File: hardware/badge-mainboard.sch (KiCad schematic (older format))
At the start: 13 parts

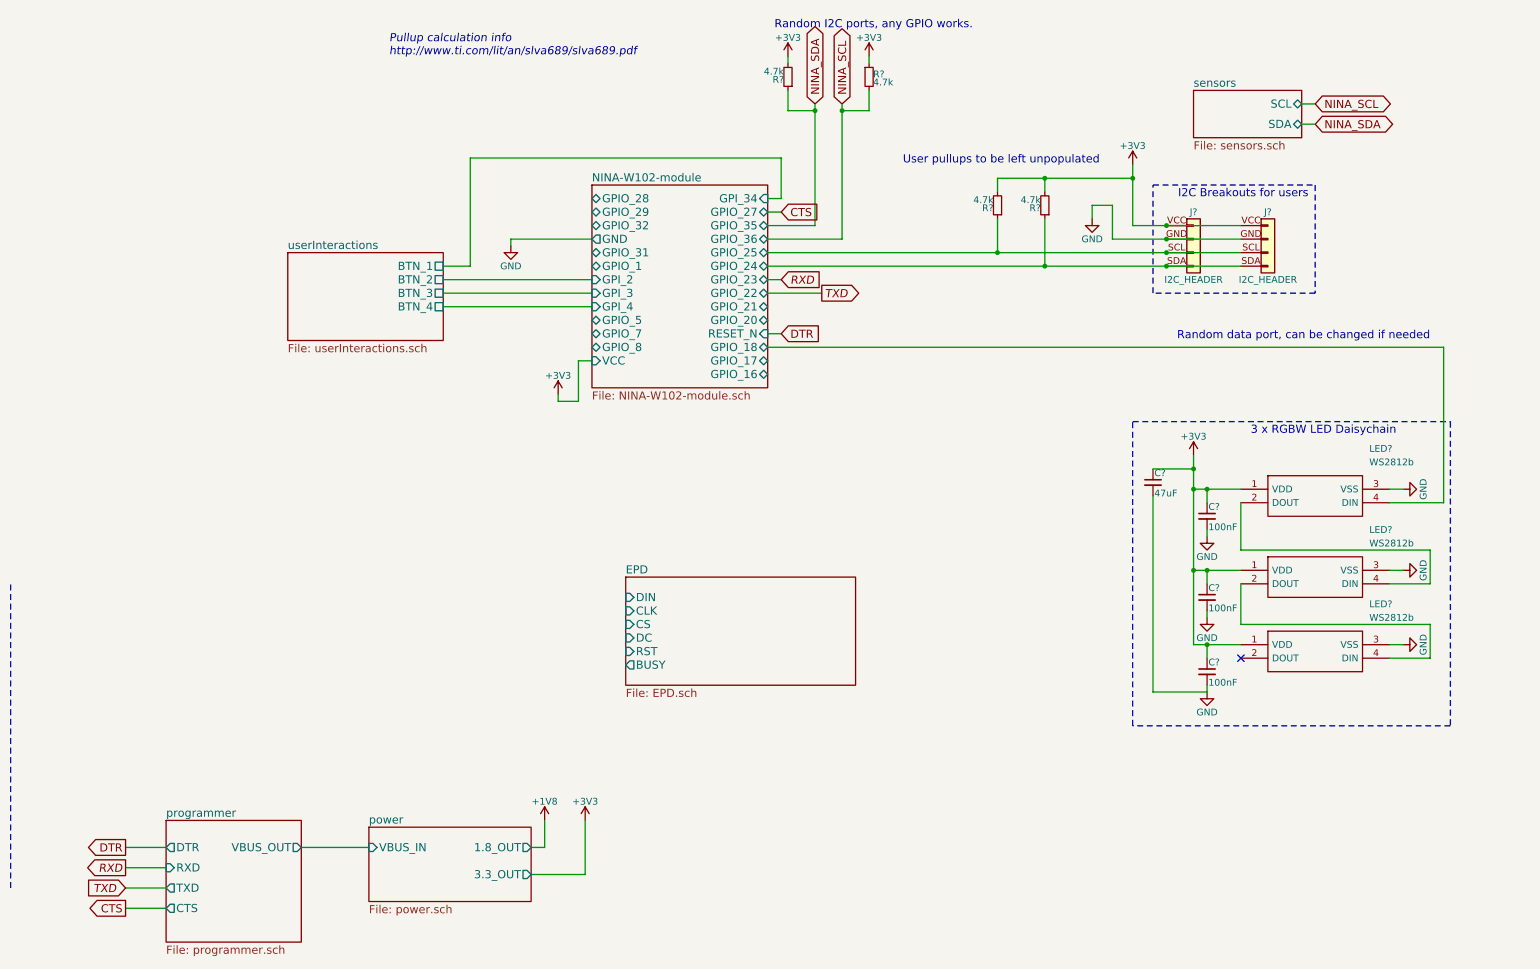
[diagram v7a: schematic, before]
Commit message: moved sensor to module board, removed programmer as external will be used
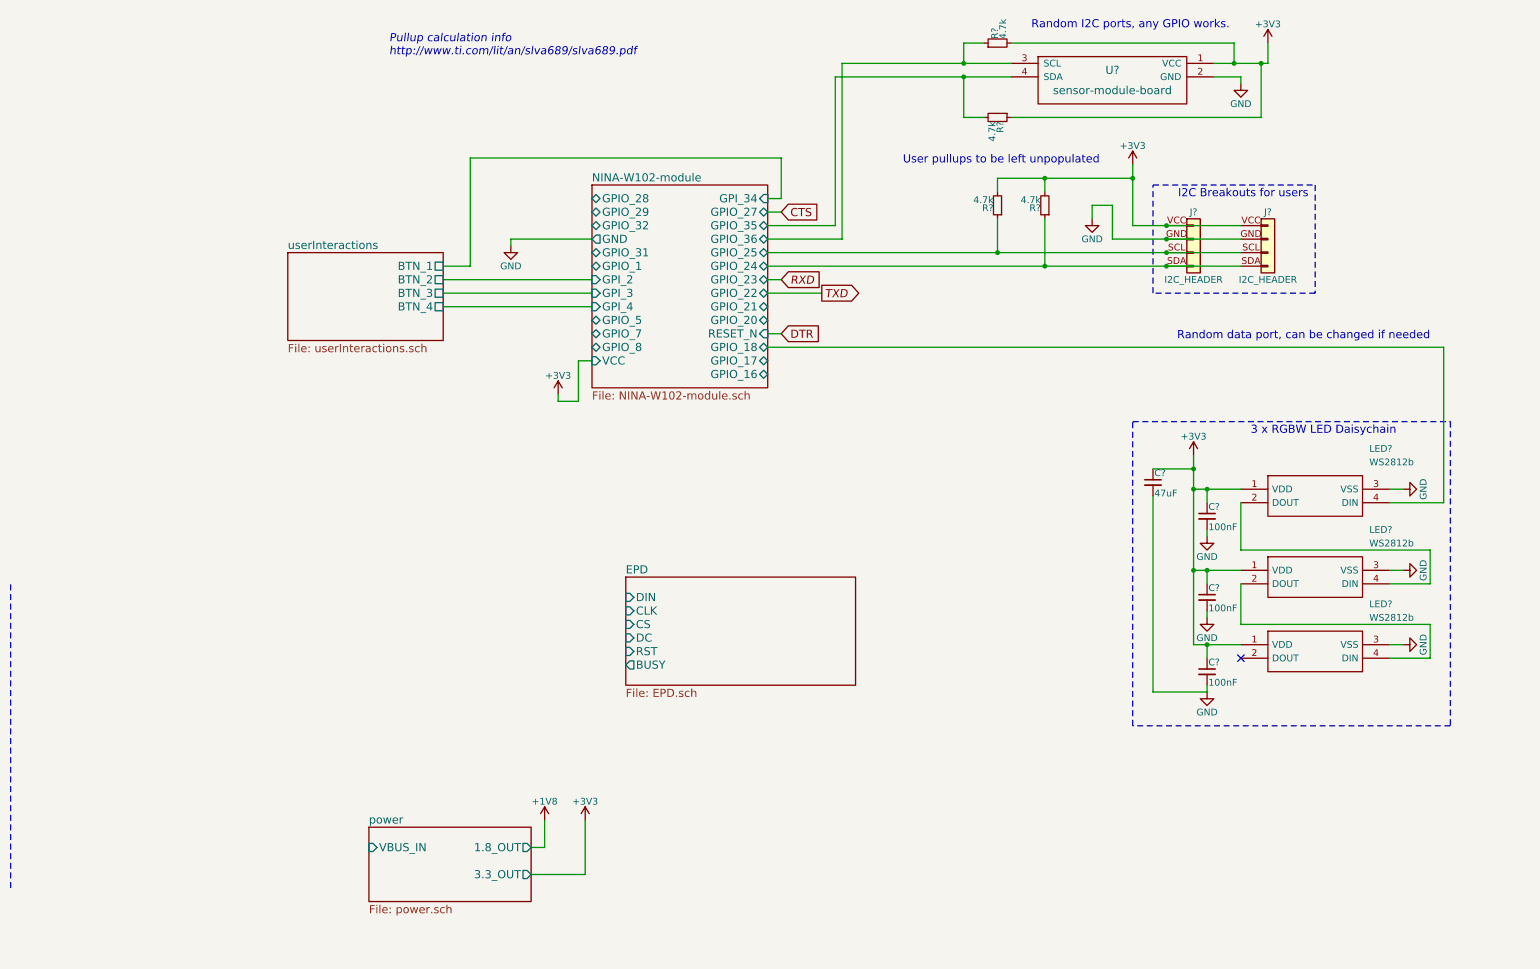
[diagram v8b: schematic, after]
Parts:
- added U?: sensor-module-board, symbol sensor-module-board
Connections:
- net +3V3: now also U?.1 (VCC)
- net GND: now also U?.2 (GND)
- net NINA_SCL renamed NINA-W102-module/GPIO_35
- net NINA-W102-module/GPIO_35: now also U?.4 (SDA)
- net NINA_SDA renamed NINA-W102-module/GPIO_36
- net NINA-W102-module/GPIO_36: now also U?.3 (SCL)
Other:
- moved on the sheet: R?
